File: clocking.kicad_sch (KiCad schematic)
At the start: 41 parts

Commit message: Schematic is basically feature complete
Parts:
- added C41: 0u1, Capacitor_SMD:C_0402_1005Metric, symbol Device:C
- added C45: 10u, Capacitor_SMD:C_0402_1005Metric, symbol Device:C
- added L40: 220, Inductor_SMD:L_0603_1608Metric, symbol Device:L_Ferrite
- added R31: 10k, symbol Device:R
- added R36: 1k, Resistor_SMD:R_0603_1608Metric, symbol Device:R
- added U31: TMP117xxDRV, Package_SON:WSON-6-1EP_2x2mm_P0.65mm_NoEP, symbol Parts:TMP117xxDRV
- C31, C32, C33, C34, C35, C36, C37, C38, C39, C44, C50, C56: renamed from C?; JLCPCB (none) -> C15525
- L31, L32, L33, L34, L35, L36, L37, L38, L39: renamed from L?; footprint (none) -> Inductor_SMD:L_0603_1608Metric; JLCPCB (none) -> C14709
- R40: renamed from R?; footprint (none) -> Inductor_SMD:L_0603_1608Metric; JLCPCB (none) -> C14709
- R41: renamed from R?; footprint 0603? -> (none)
- TP31, TP32: renamed from TP?; now left out of the parts list
- U2: renamed from U?; JLCPCB (none) -> C2891970
- U3: renamed from U?; JLCPCB (none) -> C3611586
- gave numbers to parts that had none: 14
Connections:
- net GPIO1 is gone; now on net GND: U3.24 (GPIO1)
- net CGEN_3V3: now also C41.1, R31.2, U31.4 (ADD0), U31.5 (V+)
- net GND: now also C44.1, U2.4 (GND), C41.2, C45.2, U31.2 (GND)
- net I2C_SCL: now also U31.1 (SCL)
- net I2C_SDA: now also U31.6 (SDA)
- net VDD_DIG: now also R36.2
- net GPIO0: no longer names the net of U3.12 (GPIO0)
- net GPIO0: now also R36.1
- net TXCO_3V3: no longer names the net of C46.1, R37.2, U2.9 (VCC)
- net TXCO_3V3: now also C45.1, L40.2
- new net Alert: R31.1, U31.3 (ALERT)
- new net TCXO_3V3: L40.1
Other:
- note added: "TODO - tweak foot print."
- moved on the sheet: C31, C32, C33, C34, C35, C36, C37, C38, C39, C40, C42, C43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

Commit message: Sorting out the part placement....
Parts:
- added unit 2 of U2
- L31, L32, L33, L34, L35, L36, L37, L38, L39, L40: symbol Device:L_Ferrite -> Parts:L_Ferrite_Power
- R31: footprint (none) -> Resistor_SMD:R_0402_1005Metric
- R32, R35: value ? -> 200; footprint (none) -> Resistor_SMD:R_0603_1608Metric
- R33, R34: value ? -> 100; footprint (none) -> Resistor_SMD:R_0603_1608Metric
- R39: footprint (none) -> Resistor_SMD:R_0603_1608Metric
- R40: value 220 -> 100
- R41: value 100 -> 66; footprint (none) -> Resistor_SMD:R_0603_1608Metric; now not fitted
- TP31, TP32: footprint (none) -> Parts:TestPoint
- U2: footprint QFN10_TG5032CGN -> Parts:QFN10_TG5032CGN 40.0000M-CAGHNA0_EPS; JLCPCB C2891970 -> (none)
- U3: footprint VQFN48_RGZ_TEX -> Package_DFN_QFN:QFN-48-1EP_7x7mm_P0.5mm_EP5.1x5.1mm
- U31: footprint Package_SON:WSON-6-1EP_2x2mm_P0.65mm_NoEP -> Parts:WSON-6-1EP_2x2mm_P0.65mm_NoEP
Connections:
- net GND: now also R32.1, R39.1, U3.11 (SECREF_N), U3.32 (XO_N), U3.7 (PRIREF_N); no longer R34.1, R40.1
- net GPSCLK: now also R34.1; no longer R32.1
- net SecRef: now also R41.2
- net XO: now also R40.1; no longer R39.1
- removed net XO_N: R41.2, U3.32 (XO_N)
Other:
- note added: "TODO - pads for unused outputs?"
- moved on the sheet: R32, R33, R34, R39, R40

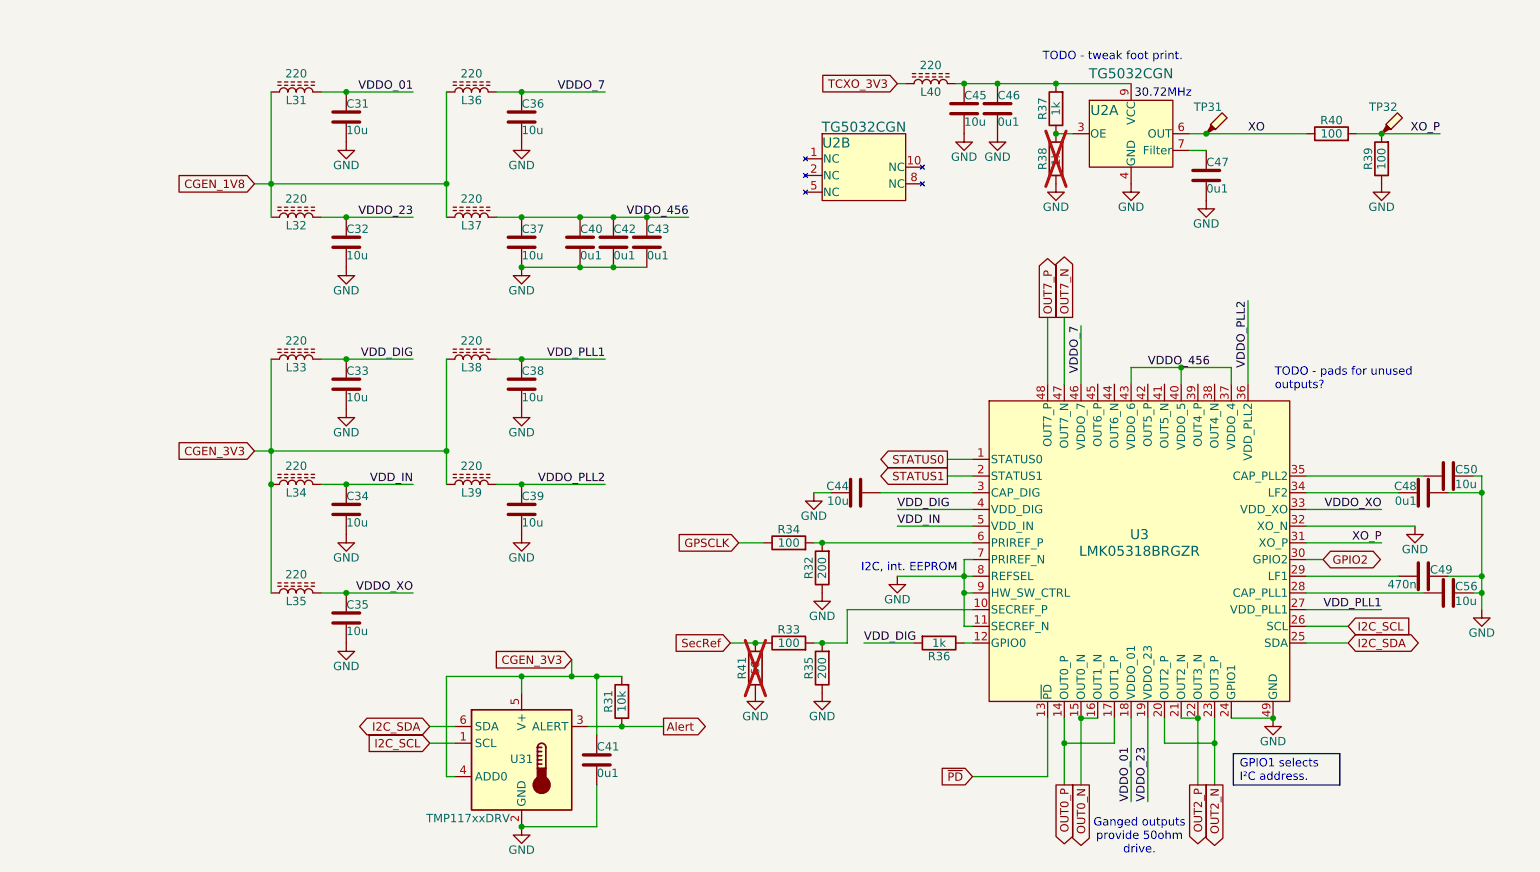
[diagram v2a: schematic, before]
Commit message: First round of component distribution
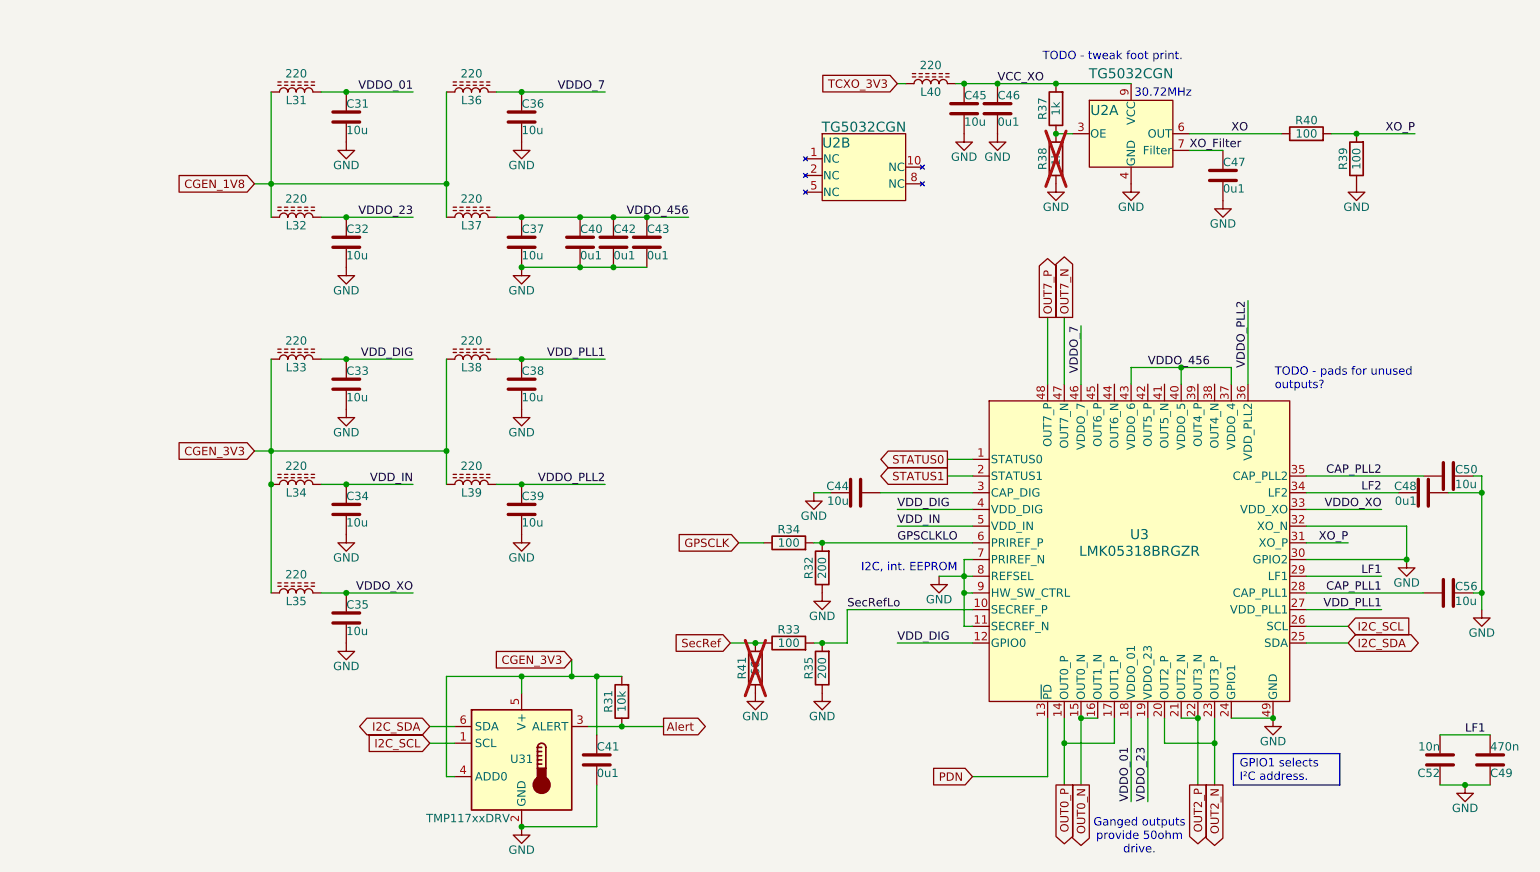
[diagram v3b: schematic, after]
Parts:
- removed R36: 1k, Resistor_SMD:R_0603_1608Metric, symbol Device:R
- removed TP31, TP32: TestPoint_Probe, Parts:TestPoint, symbol Connector:TestPoint_Probe
- added C52: 10n, Capacitor_SMD:C_0402_1005Metric_Pad0.74x0.62mm_HandSolder, symbol Device:C
- C47, C48: footprint Capacitor_SMD:C_0402_1005Metric -> Parts:C0704
- C49: footprint Capacitor_SMD:C_0402_1005Metric -> Capacitor_THT:C_Rect_L7.2mm_W3.5mm_P5.00mm_FKS2_FKP2_MKS2_MKP2
- R32, R33, R34, R35: footprint Resistor_SMD:R_0603_1608Metric -> Resistor_SMD:R_0402_1005Metric
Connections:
- net GPIO2 is gone; now on net GND: U3.30 (GPIO2)
- net GND: now also C52.2
- net VDD_DIG: now also U3.12 (GPIO0)
- net CAP_PLL2: now reaches C50.2, U3.35 (CAP_PLL2)
- net CAP_PLL1: now reaches C56.2, U3.28 (CAP_PLL1)
- net SecRefLo: now reaches R33.2, R35.2, U3.10 (SECREF_P)
- net VCC_XO: now reaches C45.1, C46.1, L40.2, R37.2, U2.9 (VCC)
- net XO_Filter: now reaches C47.1, U2.7 (Filter)
- net LF1: now reaches C49.1, U3.29 (LF1)
- net LF1: now also C52.1
- net LF2: now reaches C48.1, U3.34 (LF2)
- net GPSCLKLO: now reaches R32.2, R34.2, U3.6 (PRIREF_P)
- net ~{PD} renamed PDN
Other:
- moved on the sheet: C47, C49, R39, R40

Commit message: Routing well underway
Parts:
- added TP13: TestPoint_Probe, Parts:TestPoint, symbol Connector:TestPoint_Probe
- R37, R39: footprint Resistor_SMD:R_0603_1608Metric -> Resistor_SMD:R_0402_1005Metric
- R38: footprint Resistor_SMD:R_0603_1608Metric -> Resistor_SMD:R_0402_1005Metric; now left out of the parts list
- R40: footprint Inductor_SMD:L_0603_1608Metric -> Resistor_SMD:R_0402_1005Metric; JLCPCB C14709 -> (none)
- U31: footprint Parts:WSON-6-1EP_2x2mm_P0.65mm_NoEP -> Package_SON:WSON-6-1EP_2x2mm_P0.65mm_EP1x1.6mm
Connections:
- net GND: now also U31.7 (GND)
- net GPSCLKLO: now also TP13.1

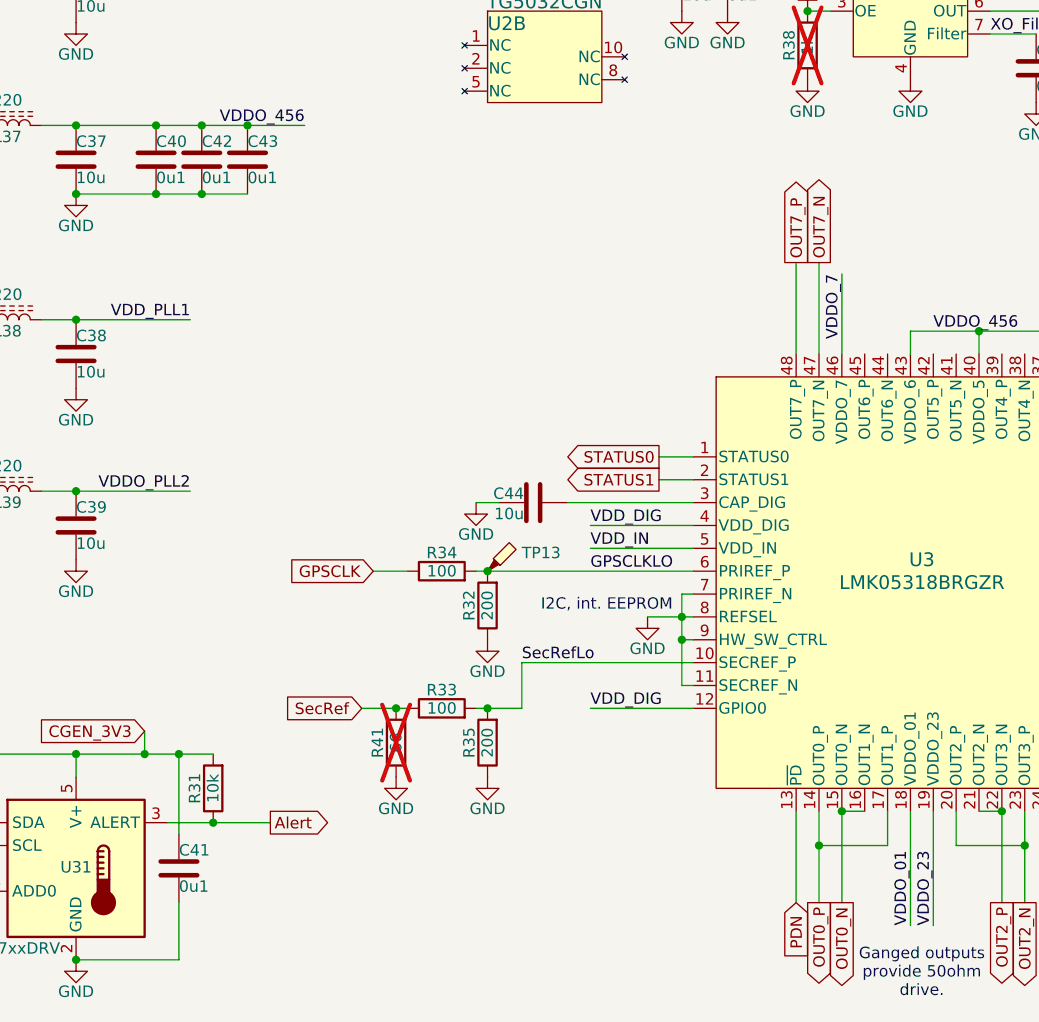
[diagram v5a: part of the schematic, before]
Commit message: Supercap is back
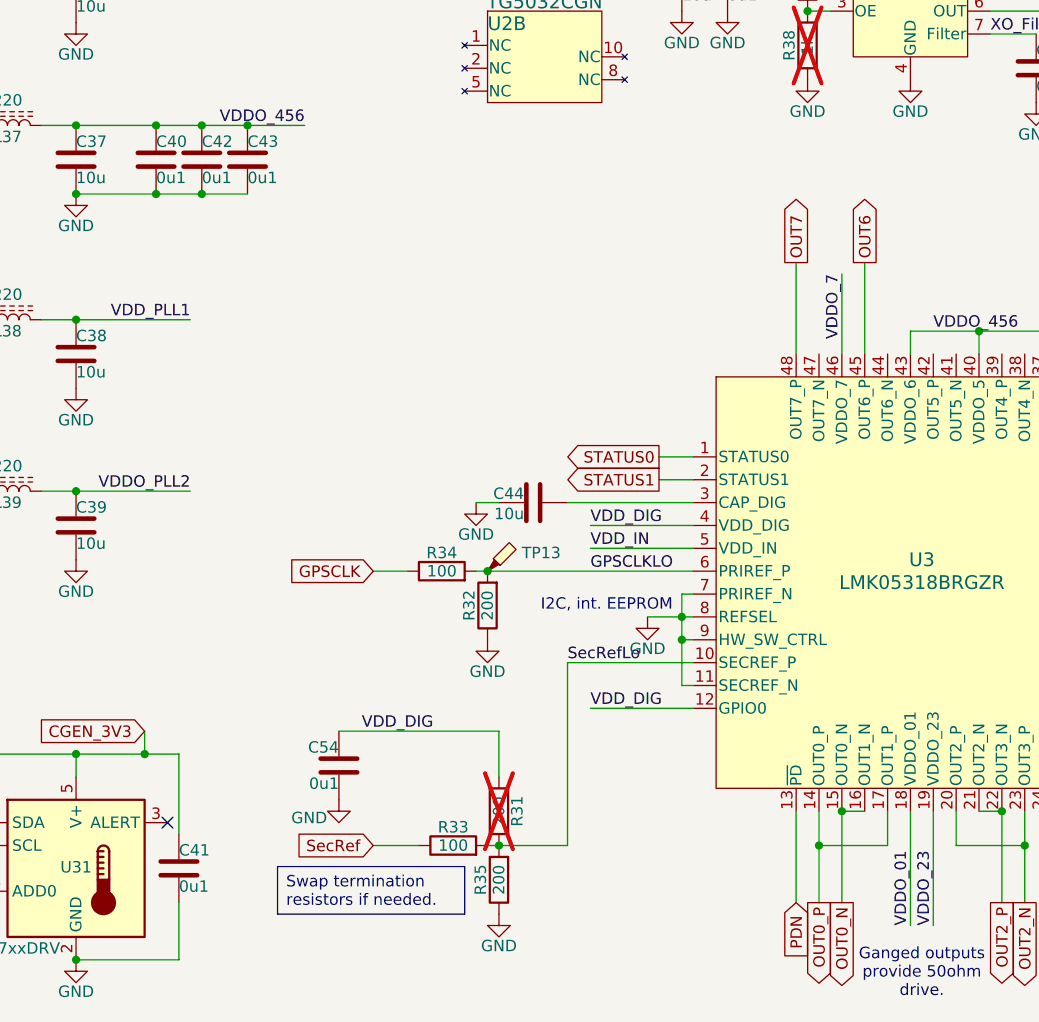
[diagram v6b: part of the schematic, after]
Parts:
- removed R41: 66, Resistor_SMD:R_0603_1608Metric, symbol Device:R
- added C54: 0u1, Capacitor_SMD:C_0402_1005Metric, symbol Device:C
- R31: value 10k -> 200; footprint Resistor_SMD:R_0402_1005Metric -> Resistor_SMD:R_0603_1608Metric; now not fitted
- R33, R35: footprint Resistor_SMD:R_0402_1005Metric -> Resistor_SMD:R_0603_1608Metric
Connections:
- net CGEN_3V3: no longer R31.2
- net GND: now also C54.2
- net SecRefLo: now also R31.1
- net VDD_DIG: now also R31.2, C54.1
- net OUT6: now reaches U3.45 (OUT6_P)
- net Alert: no longer names the net of U31.3 (ALERT)
- net Alert: no longer R31.1
- net OUT7_N: no longer names the net of U3.47 (OUT7_N)
- net OUT7_P renamed OUT7
- no-connect marks 0 -> 1
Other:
- moved on the sheet: R33, R35

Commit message: Down to the dregs and clean-ups.
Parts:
- C40, C42, C43, C46, C54: JLCPCB (none) -> C307331
- C47, C48, C49, C52, R31: now left out of the parts list
- R32: JLCPCB (none) -> C25087
- R33: JLCPCB (none) -> C22775
- R34, R39, R40: JLCPCB (none) -> C25076
- R35: JLCPCB (none) -> C8218
- R37: JLCPCB (none) -> C11702
- U2: JLCPCB (none) -> C2891970
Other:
- note removed: "TODO - tweak foot print."
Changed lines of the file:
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@@
 		)
 	)
-	(text "TODO - tweak foot print."
-		(exclude_from_sim no)
-		(at 187.198 28.956 0)
-		(effects
-			(font
-				(size 1.27 1.27)
-			)
-			(justify left)
-		)
-	)
 	(text_box "Swap termination resistors if needed."
 		(exclude_from_sim no)
@@
 			)
 		)
-		(property "JLCPCB" ""
+		(property "JLCPCB" "C8218"
 			(at 154.94 137.16 0)
 			(effects
@@
 		(unit 1)
 		(exclude_from_sim no)
-		(in_bom yes)
+		(in_bom no)
 		(on_board yes)
 		(dnp yes)
@@
 			)
 		)
+		(property "JLCPCB" "C307331"
+			(at 127 57.15 0)
+			(effects
+				(font
+					(size 1.27 1.27)
+				)
+				(hide yes)
+			)
+		)
 		(pin "1"
 		)
@@
 		(unit 1)
 		(exclude_from_sim no)
-		(in_bom yes)
+		(in_bom no)
 		(on_board yes)
 		(dnp no)
@@
 			)
 		)
+		(property "JLCPCB" "C307331"
+			(at 180.34 36.83 0)
+			(effects
+				(font
+					(size 1.27 1.27)
+				)
+				(hide yes)
+			)
+		)
 		(pin "1"
 		)
@@
 			)
 		)
-		(property "Datasheet" ""
+		(property "Datasheet" "~"
 			(at 119.38 135.89 0)
 			(effects
@@
 		(unit 1)
 		(exclude_from_sim no)
-		(in_bom yes)
+		(in_bom no)
 		(on_board yes)
 		(dnp no)
@@
 			)
 		)
+		(property "JLCPCB" "C307331"
+			(at 137.16 124.46 0)
+			(effects
+				(font
+					(size 1.27 1.27)
+				)
+				(hide yes)
+			)
+		)
 		(pin "1"
 		)
@@
 			)
 		)
-		(property "JLCPCB" ""
+		(property "JLCPCB" "C25076"
 			(at 227.33 40.64 90)
 			(effects
@@
 			)
 		)
+		(property "JLCPCB" "C307331"
+			(at 121.92 57.15 0)
+			(effects
+				(font
+					(size 1.27 1.27)
+				)
+				(hide yes)
+			)
+		)
 		(pin "1"
 		)
@@
 			)
 		)
+		(property "JLCPCB" "C307331"
+			(at 116.84 57.15 0)
+			(effects
+				(font
+					(size 1.27 1.27)
+				)
+				(hide yes)
+			)
+		)
 		(pin "1"
 		)
@@
 			)
 		)
-		(property "JLCPCB" ""
+		(property "JLCPCB" "C25076"
 			(at 234.95 44.45 0)
 			(effects
@@
 			)
 		)
-		(property "JLCPCB" ""
+		(property "JLCPCB" "C25076"
 			(at 148.59 102.87 0)
 			(effects
@@
 			)
 		)
-		(property "Datasheet" ""
+		(property "Datasheet" "~"
 			(at 189.23 44.45 0)
 			(effects
@@
 			)
 		)
-		(property "JLCPCB" ""
+		(property "JLCPCB" "C2891970"
 			(at 200.66 40.64 0)
 			(effects
@@
 			)
 		)
-		(property "JLCPCB" ""
+		(property "JLCPCB" "C22775"
 			(at 149.86 133.35 0)
 			(effects
@@
 			)
 		)
-		(property "JLCPCB" ""
+		(property "JLCPCB" "C25087"
 			(at 153.67 106.68 0)
 			(effects
@@
 			)
 		)
-		(property "Datasheet" ""
+		(property "Datasheet" "~"
 			(at 189.23 36.83 0)
 			(effects
@@
 			)
 		)
-		(property "JLCPCB" ""
+		(property "JLCPCB" "C11702"
 			(at 189.23 36.83 0)
 			(effects
@@
 			)
 		)
-		(property "JLCPCB" ""
+		(property "JLCPCB" "C2891970"
 			(at 160.02 45.72 0)
 			(effects
@@
 		(unit 1)
 		(exclude_from_sim no)
-		(in_bom yes)
+		(in_bom no)
 		(on_board yes)
 		(dnp no)
@@
 		(unit 1)
 		(exclude_from_sim no)
-		(in_bom yes)
+		(in_bom no)
 		(on_board yes)
 		(dnp no)
@@
 			)
 		)
-		(property "Datasheet" "C0G 0704"
+		(property "Datasheet" "C0G"
 			(at 245.11 95.25 0)
 			(effects

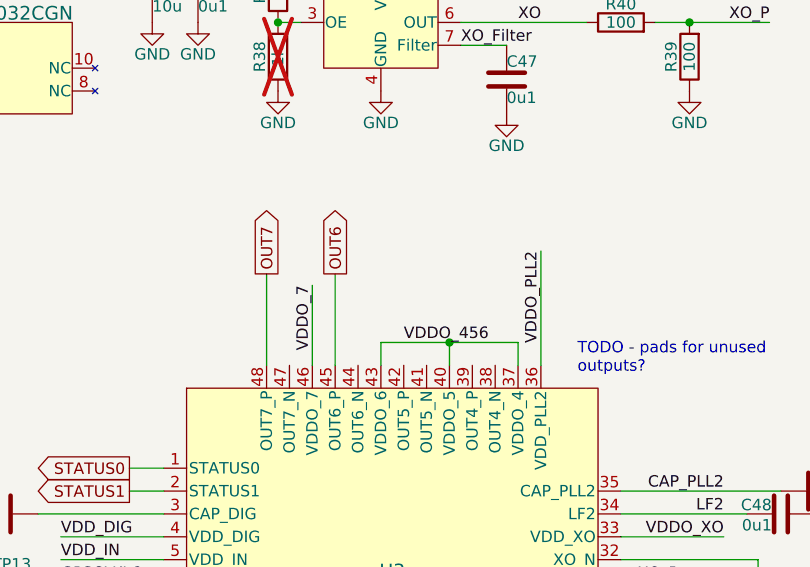
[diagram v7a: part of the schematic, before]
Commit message: Add a U.Fl connector for fun.
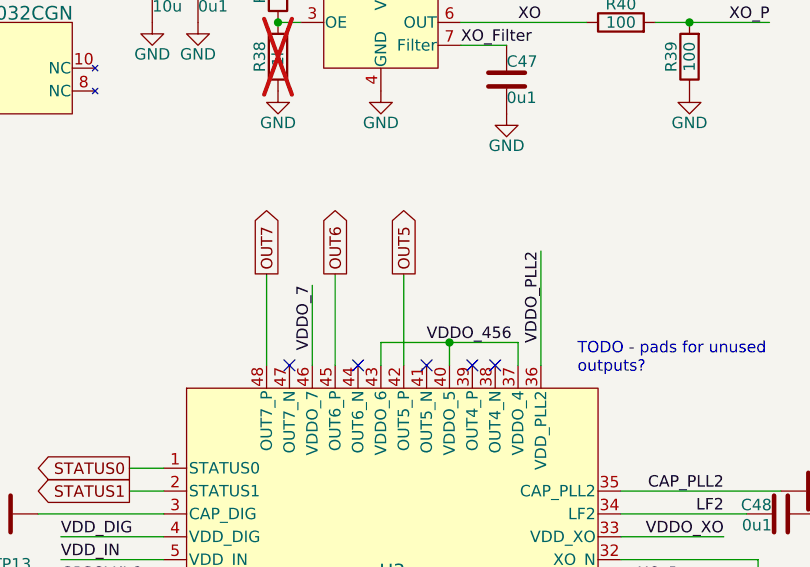
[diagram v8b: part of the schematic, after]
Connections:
- net OUT5: now reaches U3.42 (OUT5_P)
- no-connect marks 1 -> 6
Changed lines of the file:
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@@
+	)
+	(no_connect
+		(at 213.36 78.74)
+	)
+	(no_connect
+		(at 198.12 78.74)
 	)
 	(no_connect
 		(at 118.11 130.81)
 	)
+	(no_connect
+		(at 205.74 78.74)
+	)
+	(no_connect
+		(at 210.82 78.74)
+	)
+	(no_connect
+		(at 190.5 78.74)
+	)
 	(wire
 		(pts
@@
 	(wire
 		(pts
+			(xy 203.2 68.58) (xy 203.2 78.74)
+		)
+		(stroke
+			(width 0)
+			(type default)
+		)
+	)
+	(wire
+		(pts
 			(xy 93.98 133.35) (xy 97.79 133.35)
 		)
@@
 	(wire
 		(pts
-			(xy 208.28 76.2) (xy 200.66 76.2)
+			(xy 200.66 76.2) (xy 208.28 76.2)
 		)
 		(stroke
@@
 	)
 	(label "VDDO_456"
-		(at 203.2 76.2 0)
+		(at 205.74 76.2 0)
 		(effects
 			(font
@@
 			)
 		)
+	)
+	(global_label "OUT5"
+		(shape output)
+		(at 203.2 68.58 90)
+		(fields_autoplaced yes)
+		(effects
+			(font
+				(size 1.27 1.27)
+			)
+			(justify left)
+		)
+		(property "Intersheetrefs" "${INTERSHEET_REFS}"
+			(at 203.2 60.7567 90)
+			(effects
+				(font
+					(size 1.27 1.27)
+				)
+				(justify left)
+			)
+		)
